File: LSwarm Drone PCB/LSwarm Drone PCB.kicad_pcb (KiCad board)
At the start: 4 copper layers, 100 x 99.8 mm, 120 parts, among them J2 Conn_01x06_Pin, J3 JST / BT2.0 Connector, J4 Conn_01x02_Pin, J5 Conn_01x02_Pin, J6 Conn_01x02_Pin, J7 Conn_01x02_Pin, J8 Conn_01x05_Pin, Q1 AO3400A, Q2 AO3400A, Q3 AO3400A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

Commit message: sync
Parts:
- moved C55 0.40 mm to (23.8, 59.3)
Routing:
- net BATT_SW+: track 313.9 -> 379.6 mm
- net +5V: track 319.0 -> 293.5 mm
- net RP2350_GPIO_19: track 42.0 -> 46.2 mm
- net Net-(U6-3V3): track 1.81 -> 2.69 mm
- net GND: track 189.0 -> 188.8 mm, vias 109 -> 108

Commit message: sync
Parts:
- moved hackclub 0.50 mm to (36.5, 21.5)
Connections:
- J2 pad 1: RP2350_GPIO_17 -> RP2350_GPIO_0
- J2 pad 2: RP2350_GPIO_16 -> RP2350_GPIO_1
- J2 pad 3: RP2350_GPIO_14 -> RP2350_GPIO_2
- J2 pad 4: RP2350_GPIO_15 -> RP2350_GPIO_3
- R19 pad 1: Net-(U4-B) -> RP2350_GPIO_25_5.5V
- R19 pad 2: RP2350_GPIO_25_5.5V -> Net-(U4-B)
- RP2350 pad 35: RP2350_GPIO_23 -> unconnected-(RP2350-GPIO23-Pad35)
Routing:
- net RP2350_GPIO_2: track 25.6 -> 96.5 mm, vias 2 -> 3
- net RP2350_GPIO_1: track 25.0 -> 94.2 mm
- net RP2350_GPIO_0: track 25.1 -> 94.3 mm, vias 2 -> 3
- net RP2350_GPIO_3: track 16.6 -> 77.3 mm
- net +5V: track 293.5 -> 318.5 mm
- net GND: track 188.8 -> 191.1 mm, vias 108 -> 109
- net +3.3V: track 63.7 -> 65.0 mm, vias 39 -> 40

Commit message: sync
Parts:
- turned R19 to 0 degrees
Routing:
- net +1V1: track 46.3 -> 30.9 mm, vias 0 -> 4
- added copper zone on In2.Cu, net +1V1
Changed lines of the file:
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@@
 	(footprint "Resistor_SMD:R_0603_1608Metric"
 		(layer "F.Cu")
-		(at 61.95 73.9 180)
+		(at 61.95 73.9)
 		(descr "Resistor SMD 0603 (1608 Metric), square (rectangular) end terminal, IPC-7351 nominal, (Body size source: IPC-SM-782 page 72, https://www.pcb-3d.com/wordpress/wp-content/uploads/ipc-sm-782a_amendment_1_and_2.pdf)")
 		(tags "resistor")
 		(property "Reference" "R19"
-			(at 2.95 -0.1 180)
+			(at -2.95 0.1 0)
 			(layer "F.SilkS")
 			(effects
@@
 		(duplicate_pad_numbers_are_jumpers no)
 		(fp_line
-			(start -0.237258 0.5225)
-			(end 0.237258 0.5225)
+			(start -0.237258 -0.5225)
+			(end 0.237258 -0.5225)
 			(stroke
 				(width 0.12)
@@
 		)
 		(fp_line
-			(start -0.237258 -0.5225)
-			(end 0.237258 -0.5225)
+			(start -0.237258 0.5225)
+			(end 0.237258 0.5225)
 			(stroke
 				(width 0.12)
@@
 		)
 		(pad "1" smd roundrect
-			(at -0.825 0 180)
+			(at -0.825 0)
 			(size 0.8 0.95)
 			(layers "F.Cu" "F.Mask" "F.Paste")
@@
 		)
 		(pad "2" smd roundrect
-			(at 0.825 0 180)
+			(at 0.825 0)
 			(size 0.8 0.95)
 			(layers "F.Cu" "F.Mask" "F.Paste")
@@
 	)
 	(segment
-		(start 59.55525 20.16)
-		(end 59.5 20.16)
-		(width 0.2)
-		(layer "F.Cu")
-		(net "RP2350_GPIO_0")
-	)
-	(segment
 		(start 76.6391 31.320908)
 		(end 74.6891 29.370908)
@@
 	)
 	(segment
+		(start 31.25 58)
+		(end 30.235 58)
+		(width 0.2)
+		(layer "F.Cu")
+		(net "RP2350_GPIO_2")
+	)
+	(segment
 		(start 30.135 58.1)
 		(end 30.185 58.05)
@@
 	)
 	(segment
+		(start 30.235 58)
+		(end 30.185 58.05)
+		(width 0.2)
+		(layer "F.Cu")
+		(net "RP2350_GPIO_2")
+	)
+	(segment
 		(start 43.818152 49.25377)
 		(end 44.264382 49.7)
@@
 	)
 	(segment
-		(start 30.235 58)
-		(end 30.185 58.05)
-		(width 0.2)
-		(layer "F.Cu")
-		(net "RP2350_GPIO_2")
-	)
-	(segment
 		(start 39.5 49.05377)
 		(end 39.55377 49.05377)
@@
 	)
 	(segment
-		(start 31.5 58)
-		(end 30.235 58)
-		(width 0.2)
-		(layer "F.Cu")
-		(net "RP2350_GPIO_2")
-	)
-	(segment
 		(start 62.165686 29.1)
 		(end 67.363878 29.1)
@@
 	)
 	(via
-		(at 31.5 58)
+		(at 31.25 58)
 		(size 0.6)
 		(drill 0.3)
@@
 	)
 	(segment
-		(start 36.002126 49.5)
-		(end 38 49.5)
+		(start 37.901471 49.5)
+		(end 39.05377 49.5)
 		(width 0.2)
 		(layer "B.Cu")
@@
 	)
 	(segment
-		(start 33.224062 46.224878)
-		(end 33.224062 46.721936)
+		(start 36.002126 49.5)
+		(end 38 49.5)
 		(width 0.2)
 		(layer "B.Cu")
@@
 	)
 	(segment
-		(start 31.5 58)
-		(end 34.5 55)
+		(start 33.224062 46.224878)
+		(end 33.224062 46.721936)
 		(width 0.2)
 		(layer "B.Cu")
@@
 	)
 	(segment
-		(start 34.5 55)
-		(end 34.5 52.901471)
+		(start 34.5 52.901471)
+		(end 37.901471 49.5)
+		(width 0.2)
+		(layer "B.Cu")
+		(net "RP2350_GPIO_2")
+	)
+	(segment
+		(start 31.25 58)
+		(end 31.5 58)
 		(width 0.2)
 		(layer "B.Cu")
@@
 	)
 	(segment
-		(start 37.901471 49.5)
-		(end 39.05377 49.5)
+		(start 34.5 55)
+		(end 34.5 52.901471)
 		(width 0.2)
 		(layer "B.Cu")
@@
 	)
 	(segment
-		(start 34.5 52.901471)
-		(end 37.901471 49.5)
+		(start 31.5 58)
+		(end 34.5 55)
 		(width 0.2)
 		(layer "B.Cu")
@@
 	)
 	(segment
-		(start 50.05 54.25364)
-		(end 49.09636 53.3)
-		(width 0.2)
-		(layer "F.Cu")
-		(net "+1V1")
-	)
-	(segment
 		(start 51.25 47.85)
 		(end 51.25 46.618628)
@@
 	)
 	(segment
-		(start 51.25 48.5)
-		(end 52.25 49.5)
+		(start 51.25 47.85)
+		(end 51.25 49.099998)
 		(width 0.2)
 		(layer "F.Cu")
@@
 	)
 	(segment
-		(start 56.825 50.9)
-		(end 53.5 50.9)
-		(width 0.2)
-		(layer "F.Cu")
-		(net "+1V1")
-	)
-	(segment
-		(start 52.25 49.5)
-		(end 52.25 50.25)
-		(width 0.2)
-		(layer "F.Cu")
-		(net "+1V1")
-	)
-	(segment
-		(start 48.125 49.25)
-		(end 50.5 49.25)
-		(width 0.2)
-		(layer "F.Cu")
-		(net "+1V1")
-	)
-	(segment
-		(start 47.75 49.625)
-		(end 48.125 49.25)
+		(start 46.6 50.5)
+		(end 47.849998 50.5)
 		(width 0.2)
 		(layer "F.Cu")
@@
 	)
 	(segment
-		(start 52.05 51.75)
-		(end 52.9 50.9)
-		(width 0.2)
-		(layer "F.Cu")
-		(net "+1V1")
-	)
-	(segment
-		(start 47.75 49.84636)
-		(end 47.75 49.625)
-		(width 0.2)
-		(layer "F.Cu")
-		(net "+1V1")
-	)
-	(segment
-		(start 50.5 49.25)
-		(end 51.25 48.5)
+		(start 56.1 50.9)
+		(end 53.5 50.9)
 		(width 0.2)
 		(layer "F.Cu")
@@
 	)
 	(segment
-		(start 51.25 48.5)
-		(end 51.25 47.85)
+		(start 53.5 50.9)
+		(end 53.00364 50.9)
 		(width 0.2)
 		(layer "F.Cu")
@@
 	)
 	(segment
-		(start 47.09636 50.5)
-		(end 47.75 49.84636)
+		(start 53.00364 50.9)
+		(end 53.001473 50.902167)
 		(width 0.2)
 		(layer "F.Cu")
@@
 	)
 	(segment
-		(start 51.25 46.618628)
-		(end 52 45.868628)
-		(width 0.2)
-		(layer "F.Cu")
-		(net "+1V1")
-	)
-	(segment
 		(start 53.5 41.525)
 		(end 54.05 41.525)
@@
 	)
 	(segment
-		(start 51.25 54)
-		(end 52.05 53.2)
-		(width 0.2)
-		(layer "F.Cu")
-		(net "+1V1")
-	)
-	(segment
-		(start 48.05 53.3)
-		(end 47.75 53)
-		(width 0.2)
-		(layer "F.Cu")
-		(net "+1V1")
-	)
-	(segment
 		(start 54.05 41.525)
 		(end 54.375 41.85)
@@
 	)
 	(segment
-		(start 47.75 53)
-		(end 47.75 51.15364)
-		(width 0.2)
-		(layer "F.Cu")
-		(net "+1V1")
-	)
-	(segment
 		(start 47.09636 50.5)
 		(end 46.6 50.5)
@@
 	)
 	(segment
-		(start 52.25 50.25)
-		(end 52.9 50.9)
-		(width 0.2)
-		(layer "F.Cu")
-		(net "+1V1")
-	)
-	(segment
-		(start 49.09636 53.3)
-		(end 48.05 53.3)
+		(start 46.6 50.5)
+		(end 43.275 50.5)
 		(width 0.2)
 		(layer "F.Cu")
@@
 	)
 	(segment
-		(start 52.05 53.2)
-		(end 52.05 51.75)
+		(start 57.225 50.5)
+		(end 56.5 50.5)
 		(width 0.2)
 		(layer "F.Cu")
@@
 	)
 	(segment
-		(start 46.6 50.5)
-		(end 43.275 50.5)
+		(start 50.05 53.506084)
+		(end 50.05 54.75)
 		(width 0.2)
 		(layer "F.Cu")
@@
 	)
 	(segment
-		(start 50.05 54.25364)
-		(end 50.30364 54)
+		(start 51.725 46.143628)
+		(end 51.725 44.5)
 		(width 0.2)
 		(layer "F.Cu")
@@
 	)
 	(segment
-		(start 52.9 50.9)
-		(end 53.5 50.9)
+		(start 56.5 50.5)
+		(end 56.1 50.9)
 		(width 0.2)
 		(layer "F.Cu")
@@
 	)
 	(segment
-		(start 47.75 51.15364)
-		(end 47.09636 50.5)
-		(width 0.2)
-		(layer "F.Cu")
-		(net "+1V1")
-	)
-	(segment
 		(start 51.725 44.5)
 		(end 54.375 41.85)
@@
 	)
 	(segment
-		(start 52 45.868628)
-		(end 52 44.775)
-		(width 0.2)
-		(layer "F.Cu")
-		(net "+1V1")
-	)
-	(segment
 		(start 56.5 42.4)
 		(end 56.640685 42.4)
@@
 	)
 	(segment
-		(start 52 44.775)
-		(end 51.725 44.5)
+		(start 50.043918 53.500002)
+		(end 50.05 53.506084)
 		(width 0.2)
 		(layer "F.Cu")
@@
 	)
 	(segment
-		(start 57.225 50.5)
-		(end 56.825 50.9)
+		(start 53.001473 50.902167)
+		(end 52.250002 50.902167)
 		(width 0.2)
 		(layer "F.Cu")
@@
 	)
 	(segment
-		(start 50.30364 54)
-		(end 51.25 54)
+		(start 51.25 46.618628)
+		(end 51.725 46.143628)
 		(width 0.2)
 		(layer "F.Cu")
 		(net "+1V1")
 	)
+	(via
+		(at 52.250002 50.902167)
+		(size 0.6)
+		(drill 0.3)
+		(layers "F.Cu" "B.Cu")
+		(net "+1V1")
+	)
+	(via
+		(at 51.25 49.099998)
+		(size 0.6)
+		(drill 0.3)
+		(layers "F.Cu" "B.Cu")
+		(net "+1V1")
+	)
+	(via
+		(at 47.849998 50.5)
+		(size 0.6)
+		(drill 0.3)
+		(layers "F.Cu" "B.Cu")
+		(net "+1V1")
+	)
+	(via
+		(at 50.043918 53.500002)
+		(size 0.6)
+		(drill 0.3)
+		(layers "F.Cu" "B.Cu")
+		(net "+1V1")
+	)
 	(segment
 		(start 43.995901 51.285639)
@@
 			)
 		)
+	)
+	(zone
+		(net "+1V1")
+		(layer "In2.Cu")
+		(hatch edge 0.5)
+		(priority 1)
+		(connect_pads
+			(clearance 0.5)
+		)
+		(min_thickness 0.1)
+		(fill yes
+			(thermal_gap 0.5)
+			(thermal_bridge_width 0.5)
+			(island_removal_mode 1)
+		)
+		(polygon
+			(pts
+				(xy 47.528598 48.754296) (xy 47.528598 53.835142) (xy 52.570842 53.835142) (xy 52.570842 48.754296)
+			)
+		)

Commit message: sync
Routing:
- net GND: vias 109 -> 112
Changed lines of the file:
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@@
+	)
+	(via
+		(at 51.043901 50.198915)
+		(size 0.6)
+		(drill 0.3)
+		(layers "F.Cu" "B.Cu")
+		(net "GND")
 	)
 	(via
@@
 	)
 	(via
+		(at 49.043901 52.448915)
+		(size 0.6)
+		(drill 0.3)
+		(layers "F.Cu" "B.Cu")
+		(net "GND")
+	)
+	(via
 		(at 53.501517 65.021552)
 		(size 1.2)
@@
 	)
 	(via
-		(at 50.05 51.3)
-		(size 0.6)
-		(drill 0.3)
-		(layers "F.Cu" "B.Cu")
-		(net "GND")
-	)
-	(via
 		(at 20.32041 55.5224)
 		(size 0.6)
@@
 	)
 	(via
+		(at 49.043901 50.198915)
+		(size 0.6)
+		(drill 0.3)
+		(layers "F.Cu" "B.Cu")
+		(net "GND")
+	)
+	(via
 		(at 61.75 63.25)
 		(size 0.6)
 		(drill 0.3)
+		(layers "F.Cu" "B.Cu")
+		(net "GND")
+	)
+	(via
+		(at 51.043901 52.448915)
+		(size 0.6)
+		(drill 0.3)

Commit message: sync
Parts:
- added dino: LOGO, dino:dino, B.Cu at (62.5, 65.2)
- added dino: LOGO, dino:dino, B.Cu at (28.5, 54.8)
- added dino: LOGO, dino:dino, B.Cu at (69.2, 48.9)
- added dino: LOGO, dino:dino, B.Cu at (74.7, 20.9)
- added dino: LOGO, dino:dino, B.Cu at (78.8, 58.1)
- added dino: LOGO, dino:dino, B.Cu at (18.7, 68.3)
- added dino: LOGO, dino:dino, B.Cu at (74.3, 69.1)
- added dino: LOGO, dino:dino, B.Cu at (83.1, 73.9)
- added dino: LOGO, dino:dino, B.Cu at (65.6, 36.4)
- added dino: LOGO, dino:dino, B.Cu at (30.1, 20.9)
- added dino: LOGO, dino:dino, B.Cu at (68.2, 37.1)
- added dino: LOGO, dino:dino, B.Cu at (29.2, 79.0)
- added dino: LOGO, dino:dino, B.Cu at (83.8, 20.2)
- added dino: LOGO, dino:dino, B.Cu at (60.1, 40.3)
- added dino: LOGO, dino:dino, B.Cu at (39.6, 35.7)
- added dino: LOGO, dino:dino, B.Cu at (35.5, 62.5)
- added dino: LOGO, dino:dino, B.Cu at (29.8, 31.6)
- added dino: LOGO, dino:dino, B.Cu at (18.4, 27.2)
- added dino: LOGO, dino:dino, B.Cu at (47.5, 53.8)
- added dino: LOGO, dino:dino, B.Cu at (61.1, 25.1)
- moved J3 1.26 mm to (49.2, 78.7)
- moved Q7 1.26 mm to (50.2, 75.4)
- moved R17 1.26 mm to (45.5, 75.2)
- moved R28 1.26 mm to (47.2, 75.2)
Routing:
- net Net-(R17-Pad1): track 49.6 -> 50.8 mm

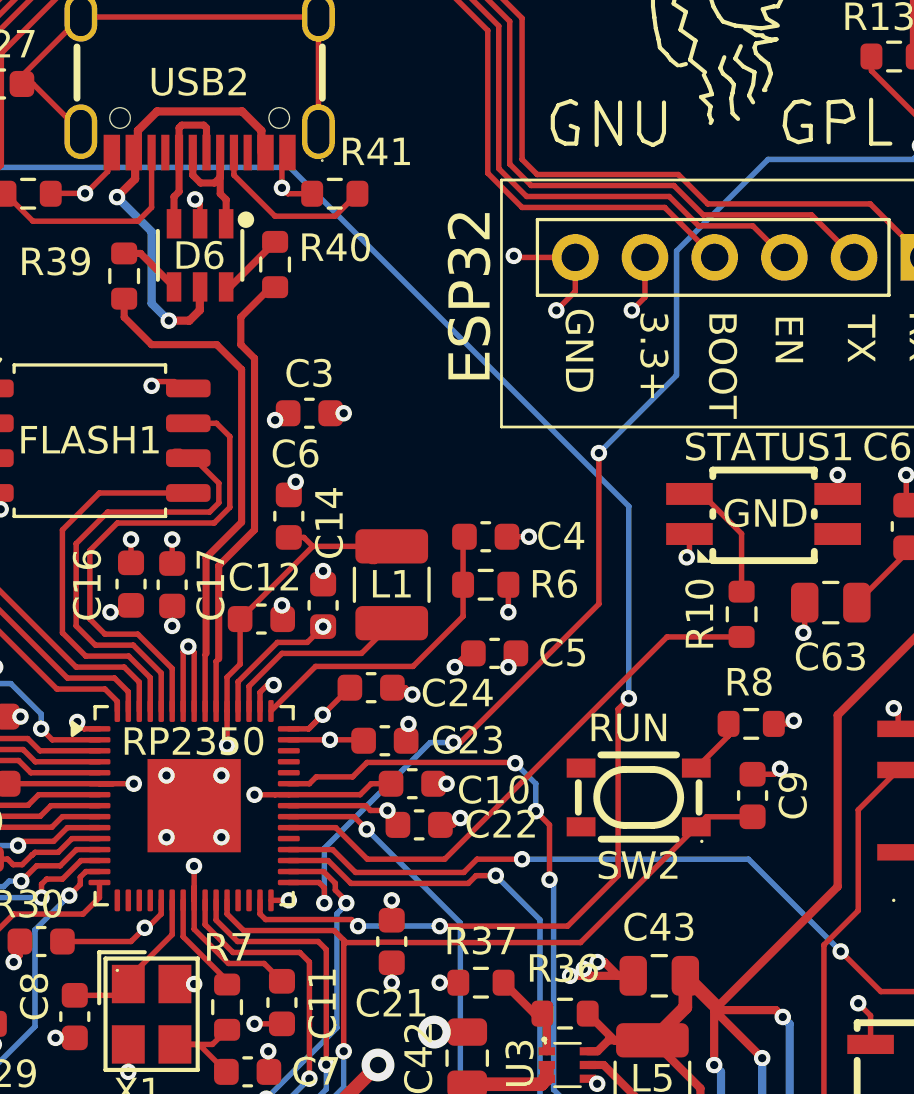
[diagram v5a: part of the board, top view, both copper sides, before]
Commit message: added vbus connection to rp2350
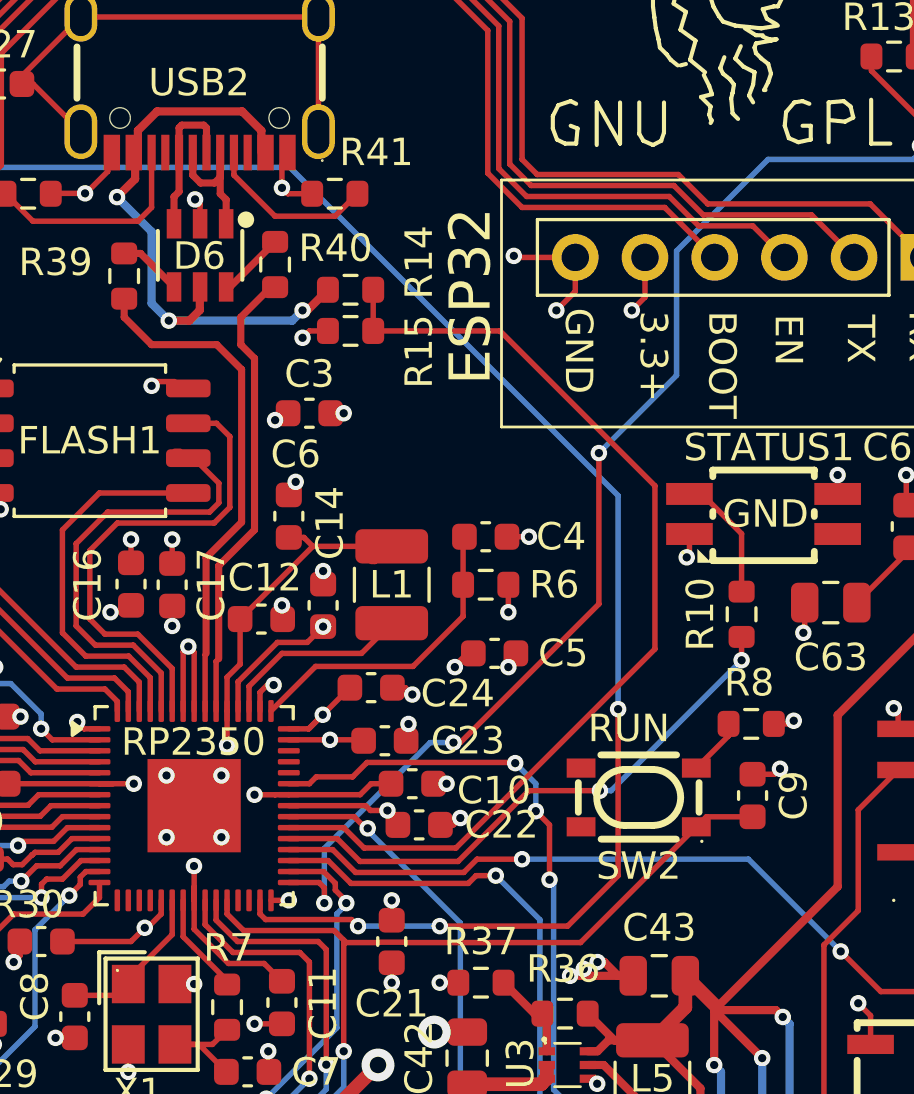
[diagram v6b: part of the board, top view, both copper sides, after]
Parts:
- added R14: 100k, Resistor_SMD:R_0603_1608Metric, F.Cu at (55.8, 32.5)
- added R15: 100k, Resistor_SMD:R_0603_1608Metric, F.Cu at (55.8, 34.0)
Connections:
- R10 pad 2: RP2350_GPIO_24 -> RP2350_GPIO_23
- RP2350 pad 35: unconnected-(RP2350-GPIO23-Pad35) -> RP2350_GPIO_23
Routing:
- net RP2350_GPIO_23: track 0.00 -> 20.7 mm, vias 0 -> 2
- net RP2350_GPIO_24: track 20.3 -> 36.7 mm
- net USB_VBUS: track 15.6 -> 21.9 mm, vias 2 -> 3
- net GND: track 191.1 -> 192.1 mm, vias 112 -> 113
